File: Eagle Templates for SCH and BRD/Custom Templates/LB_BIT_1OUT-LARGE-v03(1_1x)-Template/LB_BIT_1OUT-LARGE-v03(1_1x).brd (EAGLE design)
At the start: 21.4 x 29.1 mm, 9 parts, among them P1BSF1 BITSNAP_V03_FEMALE, U6 LV321SOT23-5

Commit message: added bitlab logo and made minor changes to board templates. Updated littlebits library.
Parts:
- added U$1: (no value), LITTLEBITS:BITLAB-LOGO
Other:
- board text added: "pX Name Here"
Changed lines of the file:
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@@
 <wire x1="19.952" y1="25.607" x2="19.952" y2="26.623" width="0.1016" layer="146"/>
 <text x="-5.65" y="-27" size="1.778" layer="46">1mm DIA. ROUTER PATH</text>
+<text x="21.3" y="16.4" size="1.3" layer="21" font="vector" rot="SR270" align="center">pX Name Here</text>
 </plain>
 <attributes>
@@
 <element name="U$4" library="LITTLEBITS" package="OSHWCREDIT" value="OSHWCREDIT" x="-94.46" y="-62.825"/>
 <element name="FRAME1" library="LITTLEBITS" package="FABDWG01-OHW" value="FRAME-LETTER" x="0" y="0"/>
+<element name="U$1" library="LITTLEBITS" package="BITLAB-LOGO" value="" x="19.8" y="21.1" rot="R270"/>
 </elements>
 <signals>

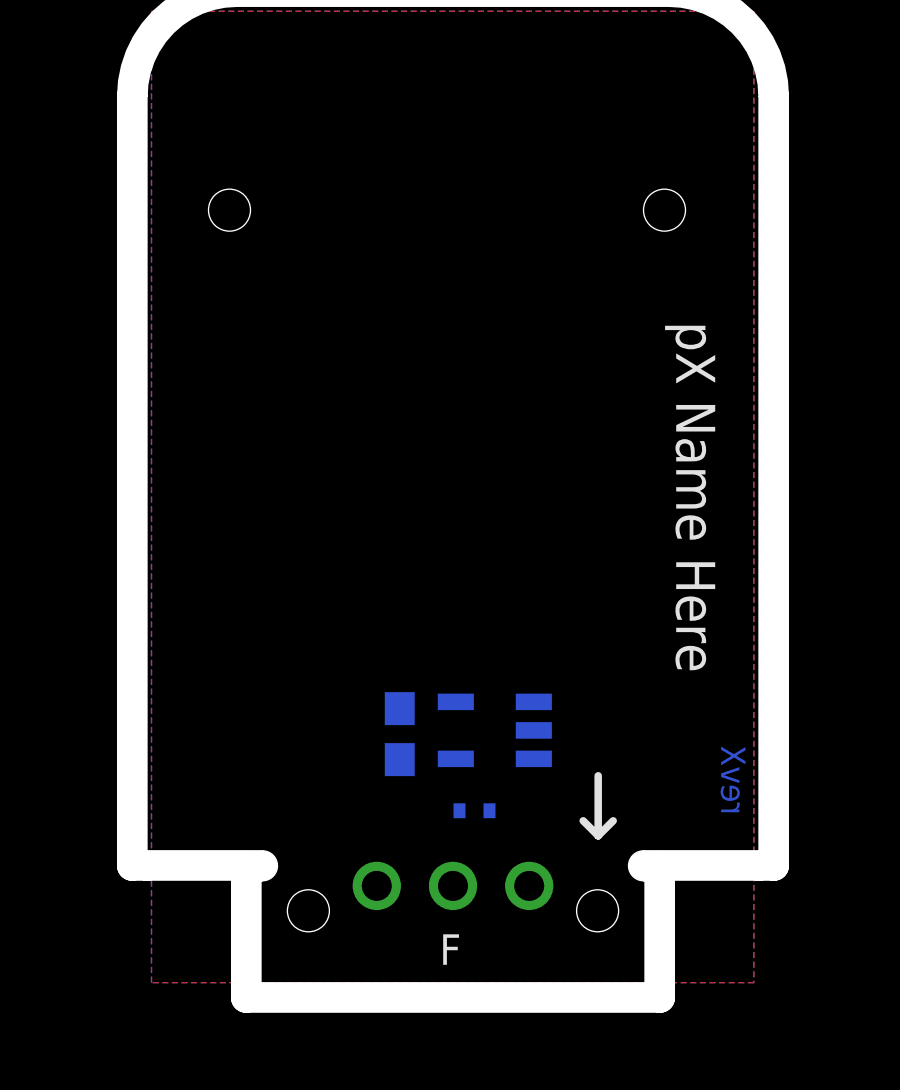
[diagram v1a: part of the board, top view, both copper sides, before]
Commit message: Updated templates
- Added ferrite beads
- Moved text and annotations off of Nets layer
- Minor layout changes
- Removed I/O/W prefix from reference designators
- Removed output stage components from output bits
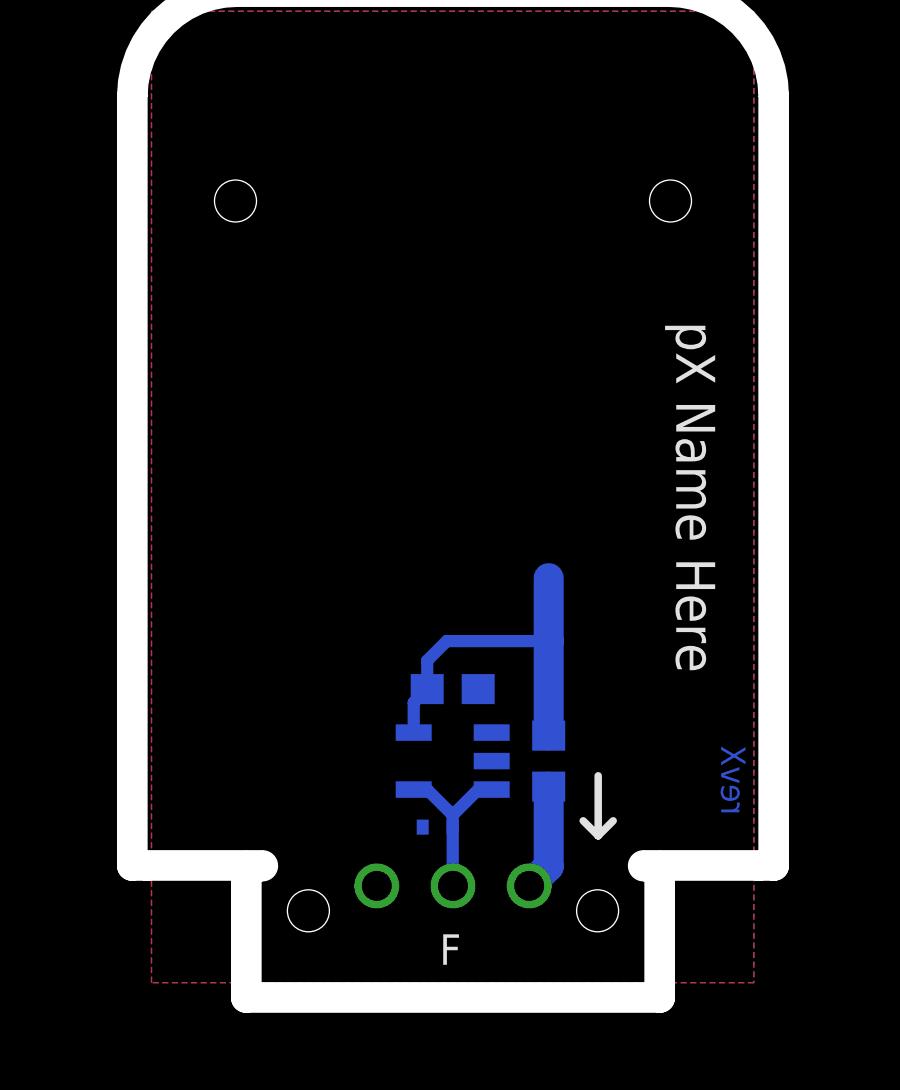
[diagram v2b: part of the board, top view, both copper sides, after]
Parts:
- removed I?C4: 1.0uF, LITTLEBITS:CAP-0603
- removed I?TVS6: ESD9B5.0ST5G, LITTLEBITS:SOD-923
- removed U6: LV321SOT23-5, LITTLEBITS:SOT23-5
- added C1: 1.0uF, LITTLEBITS:CAP-0603
- added FB1: FERRITE-BEAD0603, LITTLEBITS:R0603
- added TVS1: ESD9B5.0ST5G, LITTLEBITS:SOD-923
- added U1: LV321SOT23-5, LITTLEBITS:SOT23-5
- FRAME1: value FRAME-LETTER -> FRAME-LETTERWHITEMASK; device LITTLEBITS:FABDWG01-OHW -> LITTLEBITS:FABDWG01-WHITEMASK
- moved U$12 6.04 mm to (6.61, 26.4)
- renumbered P1BSF1 to BSF1
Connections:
- new net N$2: BSF1.VCC, FB1.1
- net GND: now also BSF1.GND, C1.1, TVS1.1, U1.2; no longer I?C4.1, I?TVS6.1, U6.2
- net N$12: now also U1.1; no longer U6.1
- net SIG_OUT: now also BSF1.SIG, TVS1.2, U1.3, U1.4; no longer I?TVS6.2, U6.3, U6.4
- net VCC: now also C1.2, FB1.2, U1.5; no longer I?C4.2, U6.5
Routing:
- net VCC: track 0.00 -> 12.2 mm
- net SIG_OUT: track 0.00 -> 5.67 mm
- net N$2: track 0.00 -> 3.58 mm
